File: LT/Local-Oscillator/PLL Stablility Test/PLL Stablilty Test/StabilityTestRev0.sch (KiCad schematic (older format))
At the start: 72 parts, among them J1 Conn_01x02_Male, J13 Conn_01x02_Male, J16 Conn_01x02_Male, J17 Conn_01x02_Male, J18 Conn_Coaxial, J2 Conn_Coaxial, J20 Conn_01x02_Male, J3 Conn_Coaxial, J4 Conn_01x04_Male, J5 Conn_01x02_Male, J7 Conn_01x02_Male, J8 Conn_01x02_Male, Q1 2N5486 JFET, Q2 2N5486 JFET, U1 LMX231X, U2 L7808

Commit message: Cleaned Up Stability Test Board
Made the schematic page bigger
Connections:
- net GND: no longer U?.3 (+)
- net at R?.1, R?.2, U?.2 (-): now also R?.1; no longer R?.2
- net at J?.1 (Pin_1): now also R?.2; no longer R?.1
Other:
- note added: "Control Voltage Vc"
- moved on the sheet: C1, C10, C11, C12, C15, C16, C17, C18, C19, C2, C20, C21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

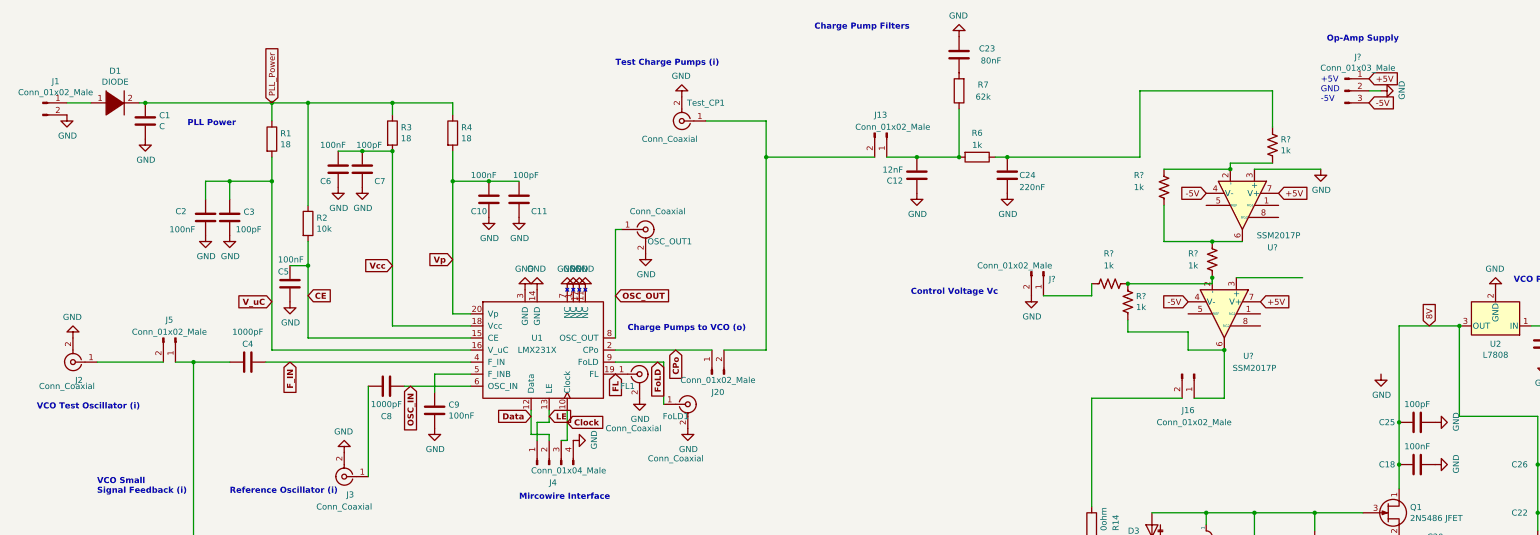
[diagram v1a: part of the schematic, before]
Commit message: Stability Test PCB design
I laid out the PCB for the stability test
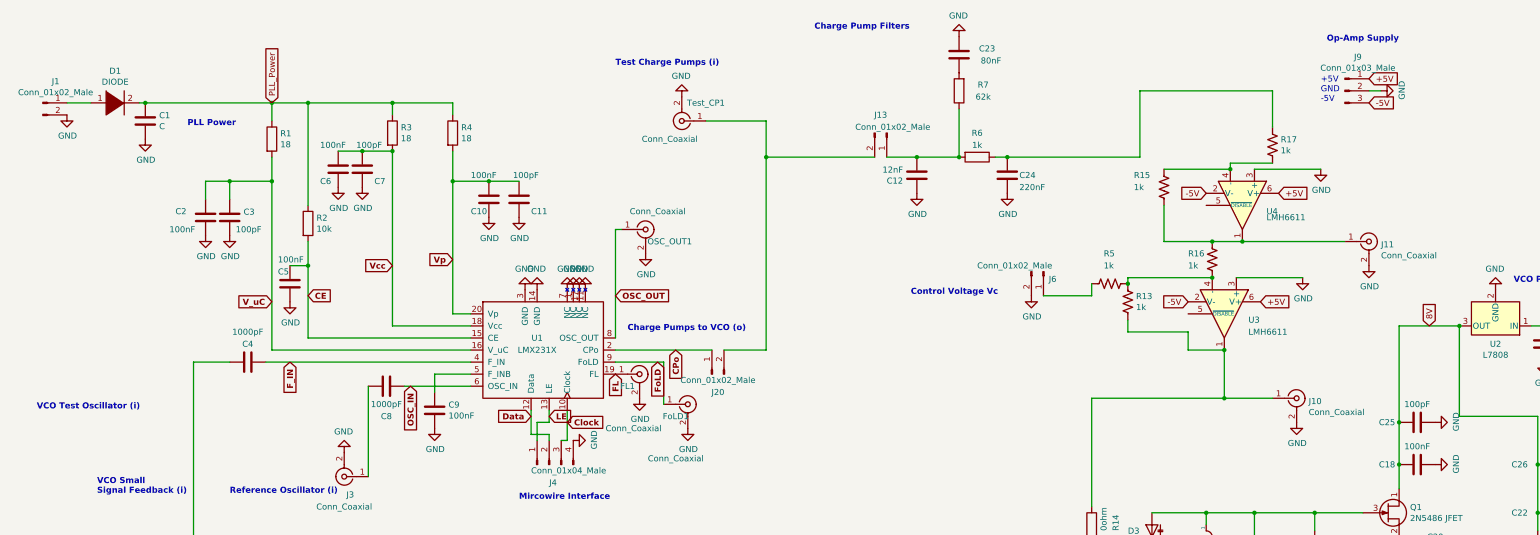
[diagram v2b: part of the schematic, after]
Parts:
- removed J16, J5: Conn_01x02_Male, Connector_PinHeader_2.54mm:PinHeader_1x02_P2.54mm_Vertical, symbol Connector:Conn_01x02_Male
- removed J2: Conn_Coaxial, Connector_Coaxial:SMA_Molex_73251-1153_EdgeMount_Horizontal, symbol Connector:Conn_Coaxial
- removed U? (x2): SSM2017P, Package_DIP:DIP-8_W7.62mm, symbol Amplifier_Audio:SSM2017P
- added J10, J11: Conn_Coaxial, Connector_Coaxial:SMA_Amphenol_132289_EdgeMount, symbol Connector:Conn_Coaxial
- added U3, U4: LMH6611, Package_TO_SOT_SMD:TSOT-23-6, symbol Amplifier_Operational:LMH6611
- J6: renamed from J?; footprint (none) -> Connector_PinHeader_2.54mm:PinHeader_1x02_P2.54mm_Vertical
- J9: renamed from J?; footprint (none) -> Connector_PinHeader_2.54mm:PinHeader_1x03_P2.54mm_Vertical
- R13, R15, R16, R17, R5: renamed from R?; footprint (none) -> Resistor_SMD:R_0805_2012Metric_Pad1.15x1.40mm_HandSolder
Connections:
- net +5V: now also U3.6 (V+), U4.6 (V+)
- net -5V: now also U3.2 (V-), U4.2 (V-)
- net GND: now also J10.2 (Ext), J11.2 (Ext), U3.3 (+), U4.3 (+)
- net at R13.2: now also R14.1, J10.1 (In), U3.1
- net at R13.1, R16.2, R5.1: now also U3.4 (-)
- net at R15.2, R17.2: now also U4.4 (-)
- net at R15.1, R16.1: now also J11.1 (In), U4.1
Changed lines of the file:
@@
 	4700 4650 4700 4800
-$Comp
-L Connector:Conn_Coaxial J2
-U 1 1 5C6B38D4
-P 1700 4550
-F 0 "J2" H 1650 4700 50  0000 C CNN
-F 1 "Conn_Coaxial" H 1750 4750 50  0000 C CNN
-F 2 "Connector_Coaxial:SMA_Molex_73251-1153_EdgeMount_Horizontal" H 1700 4550 50  0001 C CNN
-F 3 " ~" H 1700 4550 50  0001 C CNN
-	1    1700 4550
-	-1   0    0    1
-$EndComp
-$Comp
-L power:GND #PWR03
-U 1 1 5C6B3952
-P 1700 4350
-F 0 "#PWR03" H 1700 4100 50  0001 C CNN
-F 1 "GND" H 1705 4177 50  0000 C CNN
-F 2 "" H 1700 4350 50  0001 C CNN
-F 3 "" H 1700 4350 50  0001 C CNN
-	1    1700 4350
-	-1   0    0    1
-$EndComp
 $Comp
 L Connector:Conn_01x02_Male J1
@@
 	6600 4550 6600 4900
 $Comp
-L Connector:Conn_01x02_Male J5
-U 1 1 5C85A982
-P 2550 4350
-F 0 "J5" V 2400 4300 50  0000 C CNN
-F 1 "Conn_01x02_Male" V 2500 4300 50  0000 C CNN
-F 2 "Connector_PinHeader_2.54mm:PinHeader_1x02_P2.54mm_Vertical" H 2550 4350 50  0001 C CNN
-F 3 "~" H 2550 4350 50  0001 C CNN
-	1    2550 4350
-	0    1    1    0
-$EndComp
-Wire Wire Line
-	1900 4550 2450 4550
-$Comp
 L Connector:Conn_01x02_Male J7
 U 1 1 5C868E39
@@
 PLL Power
 Wire Wire Line
-	2550 4550 2700 4550
-Wire Wire Line
 	2700 4550 2700 7650
-Connection ~ 2700 4550
 Wire Wire Line
 	2700 4550 3000 4550
@@
 Clock
 $Comp
-L Connector:Conn_01x03_Male J?
+L Connector:Conn_01x03_Male J9
 U 1 1 5E57360C
 P 12250 2300
-F 0 "J?" H 12358 2581 50  0000 C CNN
+F 0 "J9" H 12358 2581 50  0000 C CNN
 F 1 "Conn_01x03_Male" H 12358 2490 50  0000 C CNN
-F 2 "" H 12250 2300 50  0001 C CNN
+F 2 "Connector_PinHeader_2.54mm:PinHeader_1x03_P2.54mm_Vertical" H 12250 2300 50  0001 C CNN
 F 3 "~" H 12250 2300 50  0001 C CNN
 	1    12250 2300
@@
 +5V\nGND\n-5V
 $Comp
-L power:GND #PWR?
+L power:GND #PWR0104
 U 1 1 5E586322
 P 12550 2300
-F 0 "#PWR?" H 12550 2050 50  0001 C CNN
+F 0 "#PWR0104" H 12550 2050 50  0001 C CNN
 F 1 "GND" H 12555 2127 50  0000 C CNN
 F 2 "" H 12550 2300 50  0001 C CNN
@@
 VCO Tuning\nVoltage (i)
 $Comp
-L power:GND #PWR?
+L power:GND #PWR0107
 U 1 1 5E5E43E2
 P 9650 4000
-F 0 "#PWR?" H 9650 3750 50  0001 C CNN
+F 0 "#PWR0107" H 9650 3750 50  0001 C CNN
 F 1 "GND" H 9655 3827 50  0000 C CNN
 F 2 "" H 9650 4000 50  0001 C CNN
@@
 $EndComp
 $Comp
-L Connector:Conn_01x02_Male J?
+L Connector:Conn_01x02_Male J6
 U 1 1 5E5E33D0
 P 9750 3800
-F 0 "J?" V 9812 3844 50  0000 L CNN
+F 0 "J6" V 9812 3844 50  0000 L CNN
 F 1 "Conn_01x02_Male" V 9700 3250 50  0000 L CNN
-F 2 "" H 9750 3800 50  0001 C CNN
+F 2 "Connector_PinHeader_2.54mm:PinHeader_1x02_P2.54mm_Vertical" H 9750 3800 50  0001 C CNN
 F 3 "~" H 9750 3800 50  0001 C CNN
 	1    9750 3800
 	0    1    1    0
 $EndComp
-Connection ~ 10450 3900
-$Comp
-L Device:R_US R?
+$Comp
+L Device:R_US R5
 U 1 1 5E5E2D3B
 P 10300 3900
-F 0 "R?" V 10050 3850 50  0000 L CNN
+F 0 "R5" V 10050 3850 50  0000 L CNN
 F 1 "1k" V 10150 3850 50  0000 L CNN
-F 2 "" V 10340 3890 50  0001 C CNN
+F 2 "Resistor_SMD:R_0805_2012Metric_Pad1.15x1.40mm_HandSolder" V 10340 3890 50  0001 C CNN
 F 3 "~" H 10300 3900 50  0001 C CNN
 	1    10300 3900
 	0    1    1    0
 $EndComp
-Connection ~ 11150 3850
-Wire Wire Line
-	11150 3900 11150 3850
-Wire Wire Line
-	10450 3900 11150 3900
 Wire Wire Line
 	11150 3550 11400 3550
 Connection ~ 11150 3550
 $Comp
-L Device:R_US R?
+L Device:R_US R16
 U 1 1 5E5D8E8D
 P 11150 3700
-F 0 "R?" H 10950 3750 50  0000 L CNN
+F 0 "R16" H 10950 3750 50  0000 L CNN
 F 1 "1k" H 10950 3650 50  0000 L CNN
-F 2 "" V 11190 3690 50  0001 C CNN
+F 2 "Resistor_SMD:R_0805_2012Metric_Pad1.15x1.40mm_HandSolder" V 11190 3690 50  0001 C CNN
 F 3 "~" H 11150 3700 50  0001 C CNN
 	1    11150 3700
 	1    0    0    -1
 $EndComp
-Connection ~ 11250 4450
 Wire Wire Line
 	10950 4450 11250 4450
@@
 	10450 4200 10450 4300
 $Comp
-L Device:R_US R?
+L Device:R_US R13
 U 1 1 5E5C96C2
 P 10450 4050
-F 0 "R?" H 10518 4096 50  0000 L CNN
+F 0 "R13" H 10518 4096 50  0000 L CNN
 F 1 "1k" H 10518 4005 50  0000 L CNN
-F 2 "" V 10490 4040 50  0001 C CNN
+F 2 "Resistor_SMD:R_0805_2012Metric_Pad1.15x1.40mm_HandSolder" V 10490 4040 50  0001 C CNN
 F 3 "~" H 10450 4050 50  0001 C CNN
 	1    10450 4050
@@
 Wire Wire Line
 	11650 2600 11650 2300
-Connection ~ 11300 2950
 Wire Wire Line
 	11300 2900 11650 2900
@@
 	10750 2950 11300 2950
 $Comp
-L Device:R_US R?
+L Device:R_US R17
 U 1 1 5E5AD2CA
 P 11650 2750
-F 0 "R?" H 11718 2796 50  0000 L CNN
+F 0 "R17" H 11718 2796 50  0000 L CNN
 F 1 "1k" H 11718 2705 50  0000 L CNN
-F 2 "" V 11690 2740 50  0001 C CNN
+F 2 "Resistor_SMD:R_0805_2012Metric_Pad1.15x1.40mm_HandSolder" V 11690 2740 50  0001 C CNN
 F 3 "~" H 11650 2750 50  0001 C CNN
 	1    11650 2750
@@
 $EndComp
 $Comp
-L Device:R_US R?
+L Device:R_US R15
 U 1 1 5E5AB6E7
 P 10750 3100
-F 0 "R?" H 11000 3000 50  0000 R CNN
+F 0 "R15" H 11000 3000 50  0000 R CNN
 F 1 "1k" H 11000 3100 50  0000 R CNN
-F 2 "" V 10790 3090 50  0001 C CNN
+F 2 "Resistor_SMD:R_0805_2012Metric_Pad1.15x1.40mm_HandSolder" V 10790 3090 50  0001 C CNN
 F 3 "~" H 10750 3100 50  0001 C CNN
 	1    10750 3100
@@
 	11500 2950 12050 2950
 $Comp
-L power:GND #PWR?
+L power:GND #PWR0108
 U 1 1 5E5A446C
 P 12050 2950
-F 0 "#PWR?" H 12050 2700 50  0001 C CNN
+F 0 "#PWR0108" H 12050 2700 50  0001 C CNN
 F 1 "GND" H 12055 2777 50  0000 C CNN
 F 2 "" H 12050 2950 50  0001 C CNN
@@
 Text GLabel 11700 3150 2    50   Input ~ 0
 +5V
-$Comp
-L Amplifier_Audio:SSM2017P U?
-U 1 1 5E55073E
-P 11400 3250
-F 0 "U?" V 11750 3500 50  0000 C CNN
-F 1 "SSM2017P" V 11650 3550 50  0000 C CNN
-F 2 "Package_DIP:DIP-8_W7.62mm" H 11400 3250 50  0001 C CNN
-F 3 "https://www.analog.com/media/en/technical-documentation/obsolete-data-sheets/139484016SSM2017.pdf" H 11400 3250 50  0001 C CNN
-	1    11400 3250
-	0    1    1    0
-$EndComp
-$Comp
-L Amplifier_Audio:SSM2017P U?
-U 1 1 5E53DFB6
-P 11250 4150
-F 0 "U?" V 11600 4350 50  0000 C CNN
-F 1 "SSM2017P" V 11700 4400 50  0000 C CNN
-F 2 "Package_DIP:DIP-8_W7.62mm" H 11250 4150 50  0001 C CNN
-F 3 "https://www.analog.com/media/en/technical-documentation/obsolete-data-sheets/139484016SSM2017.pdf" H 11250 4150 50  0001 C CNN
-	1    11250 4150
-	0    1    1    0
-$EndComp
 Connection ~ 9450 2850
 $Comp
@@
 	-1   0    0    1
 $EndComp
-$Comp
-L Connector:Conn_01x02_Male J16
-U 1 1 5C94F36F
-P 11000 4650
-F 0 "J16" V 11300 4600 50  0000 C CNN
-F 1 "Conn_01x02_Male" V 11400 4650 50  0000 C CNN
-F 2 "Connector_PinHeader_2.54mm:PinHeader_1x02_P2.54mm_Vertical" H 11000 4650 50  0001 C CNN
-F 3 "~" H 11000 4650 50  0001 C CNN
-	1    11000 4650
-	0    1    1    0
-$EndComp
 Text Notes 7850 1800 0    50   ~ 10
 Charge Pump Filters
@@
 	12700 6000 12700 6150
 $Comp
-L power:GND #PWR?
+L power:GND #PWR0109
 U 1 1 5E5C1BFD
-P 12550 4650
-F 0 "#PWR?" H 12550 4400 50  0001 C CNN
-F 1 "GND" H 12555 4477 50  0000 C CNN
-F 2 "" H 12550 4650 50  0001 C CNN
-F 3 "" H 12550 4650 50  0001 C CNN
-	1    12550 4650
+P 12450 3750
+F 0 "#PWR0109" H 12450 3500 50  0001 C CNN
+F 1 "GND" H 12455 3577 50  0000 C CNN
+F 2 "" H 12450 3750 50  0001 C CNN
+F 3 "" H 12450 3750 50  0001 C CNN
+	1    12450 3750
 	1    0    0    -1
 $EndComp
@@
 	14400 6950 14400 7700
 Wire Wire Line
-	11000 4850 11250 4850
-Wire Wire Line
 	11250 4450 11250 4850
 Wire Wire Line
 	10150 5750 10150 4850
-Wire Wire Line
-	10150 4850 10900 4850
 Wire Wire Line
 	7450 2850 8350 2850
@@
 Wire Wire Line
 	10550 2850 10550 2300
-Wire Wire Line
-	10550 2300 11650 2300
 Wire Wire Line
 	9450 2850 10550 2850
@@
 Text Notes 8650 4000 0    50   ~ 10
 Control Voltage Vc
+$Comp
+L Amplifier_Operational:LMH6611 U4
+U 1 1 5E55DBE3
+P 11400 3250
+F 0 "U4" V 11450 3450 50  0000 L CNN
+F 1 "LMH6611" V 11500 3450 50  0000 L CNN
+F 2 "Package_TO_SOT_SMD:TSOT-23-6" H 11500 3000 50  0001 L CNN
+F 3 "http://www.ti.com/lit/ds/symlink/lmh6612.pdf" H 11550 3400 50  0001 C CNN
+	1    11400 3250
+	0    1    1    0
+$EndComp
+Connection ~ 11300 2950
+$Comp
+L Amplifier_Operational:LMH6611 U3
+U 1 1 5E5688E0
+P 11250 4150
+F 0 "U3" V 11300 4350 50  0000 L CNN
+F 1 "LMH6611" V 11400 4350 50  0000 L CNN
+F 2 "Package_TO_SOT_SMD:TSOT-23-6" H 11350 3900 50  0001 L CNN
+F 3 "http://www.ti.com/lit/ds/symlink/lmh6612.pdf" H 11400 4300 50  0001 C CNN
+	1    11250 4150
+	0    1    1    0
+$EndComp
+Connection ~ 11250 4450
+Wire Wire Line
+	11150 3850 10450 3850
+Wire Wire Line
+	10450 3850 10450 3900
+Connection ~ 11150 3850
+Connection ~ 10450 3900
+$Comp
+L power:GND #PWR0110
+U 1 1 5E57E67E
+P 11900 3850
+F 0 "#PWR0110" H 11900 3600 50  0001 C CNN
+F 1 "GND" H 11905 3677 50  0000 C CNN
+F 2 "" H 11900 3850 50  0001 C CNN
+F 3 "" H 11900 3850 50  0001 C CNN
+	1    11900 3850
+	1    0    0    -1
+$EndComp
+Wire Wire Line
+	10150 4850 11250 4850
+Wire Wire Line
+	10550 2300 11650 2300
+$Comp
+L Connector:Conn_Coaxial J11
+U 1 1 5E5B37F5
+P 12450 3550
+F 0 "J11" H 12550 3525 50  0000 L CNN
+F 1 "Conn_Coaxial" H 12550 3434 50  0000 L CNN
+F 2 "Connector_Coaxial:SMA_Amphenol_132289_EdgeMount" H 12450 3550 50  0001 C CNN
+F 3 " ~" H 12450 3550 50  0001 C CNN
+	1    12450 3550
+	1    0    0    -1
+$EndComp
+Wire Wire Line
+	11400 3550 12250 3550
+Connection ~ 11400 3550
+$Comp
+L Connector:Conn_Coaxial J10
+U 1 1 5E5B8ABE
+P 11850 4850
+F 0 "J10" H 11950 4825 50  0000 L CNN
+F 1 "Conn_Coaxial" H 11950 4734 50  0000 L CNN
+F 2 "Connector_Coaxial:SMA_Amphenol_132289_EdgeMount" H 11850 4850 50  0001 C CNN
+F 3 " ~" H 11850 4850 50  0001 C CNN
+	1    11850 4850
+	1    0    0    -1
+$EndComp
+Wire Wire Line
+	11250 4850 11650 4850
+Connection ~ 11250 4850
+$Comp
+L power:GND #PWR0111
+U 1 1 5E5C16BE
+P 11850 5050
+F 0 "#PWR0111" H 11850 4800 50  0001 C CNN
+F 1 "GND" H 11855 4877 50  0000 C CNN
+F 2 "" H 11850 5050 50  0001 C CNN
+F 3 "" H 11850 5050 50  0001 C CNN
+	1    11850 5050
+	1    0    0    -1
+$EndComp
 $EndSCHEMATC
